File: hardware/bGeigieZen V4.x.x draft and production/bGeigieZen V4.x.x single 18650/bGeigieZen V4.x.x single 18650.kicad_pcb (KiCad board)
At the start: 2 copper layers, 129.4 x 64.6 mm, 13 parts, among them J1 M5 2x15 pin, J3 GPS, J4 Geiger Safepulse, J5 Extra support header, SW1 SW_SPDT

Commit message: Updated some more traces on the 4.x..x boards
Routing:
- net Net-(QIcharger1-Pin_1): track 31.7 -> 53.7 mm
- net Net-(BT1-+): track 67.9 -> 74.8 mm
- net Net-(BT1--): track 79.7 -> 78.9 mm
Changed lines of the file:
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@@
+	)
+	(segment
+		(start 199.356 84.642342)
+		(end 199.356 81.9844)
+		(width 0.5)
+		(layer "B.Cu")
+		(net 31)
 	)
 	(segment
@@
 	)
 	(segment
+		(start 182.7785 120.528)
+		(end 194.3292 120.528)
+		(width 0.5)
+		(layer "B.Cu")
+		(net 31)
+	)
+	(segment
 		(start 197.112 75.9648)
 		(end 200.6952 79.548)
@@
 	)
 	(segment
+		(start 186.0804 97.917942)
+		(end 199.356 84.642342)
+		(width 0.5)
+		(layer "B.Cu")
+		(net 31)
+	)
+	(segment
 		(start 200.6952 81.6696)
 		(end 203.86 78.5048)
@@
 	)
 	(segment
-		(start 199.356 115.5012)
-		(end 199.356 81.9844)
-		(width 0.5)
-		(layer "B.Cu")
-		(net 31)
-	)
-	(segment
 		(start 199.356 81.9844)
 		(end 198.0516 81.9844)
@@
 	)
 	(segment
-		(start 182.7785 120.528)
-		(end 194.3292 120.528)
+		(start 186.0804 112.2792)
+		(end 186.0804 97.917942)
 		(width 0.5)
 		(layer "B.Cu")
@@
 	(segment
 		(start 194.3292 120.528)
-		(end 199.356 115.5012)
+		(end 186.0804 112.2792)
 		(width 0.5)
 		(layer "B.Cu")
@@
 	)
 	(segment
+		(start 159.512 90.4736)
+		(end 150.0632 81.0248)
+		(width 0.25)
+		(layer "B.Cu")
+		(net 32)
+	)
+	(segment
+		(start 143.648 78.4848)
+		(end 146.198 81.0348)
+		(width 0.5)
+		(layer "B.Cu")
+		(net 32)
+	)
+	(segment
 		(start 149.342 75.9548)
 		(end 149.352 75.9448)
@@
 	)
 	(segment
-		(start 192.387642 102.474042)
-		(end 170.9384 81.0248)
+		(start 184.7596 110.102084)
+		(end 184.7596 93.4708)
 		(width 0.25)
 		(layer "B.Cu")
@@
 	)
 	(segment
+		(start 150.0632 81.0248)
+		(end 149.352 81.0248)
+		(width 0.25)
+		(layer "B.Cu")
+		(net 32)
+	)
+	(segment
+		(start 142.604 78.4848)
+		(end 143.648 78.4848)
+		(width 0.5)
+		(layer "B.Cu")
+		(net 32)
+	)
+	(segment
+		(start 181.7624 90.4736)
+		(end 159.512 90.4736)
+		(width 0.25)
+		(layer "B.Cu")
+		(net 32)
+	)
+	(segment
 		(start 182.707869 112.153815)
-		(end 192.387642 102.474042)
+		(end 184.7596 110.102084)
 		(width 0.25)
 		(layer "B.Cu")
@@
 	)
 	(segment
-		(start 170.9384 81.0248)
-		(end 149.352 81.0248)
+		(start 184.7596 93.4708)
+		(end 181.7624 90.4736)
 		(width 0.25)
 		(layer "B.Cu")
@@
 	)
 	(segment
+		(start 206.4397 123.5837)
+		(end 201.3089 123.5837)
+		(width 0.5)
+		(layer "B.Cu")
+		(net 33)
+	)
+	(segment
 		(start 205.181 95.9093)
 		(end 205.181 95.9092)
@@
 	)
 	(segment
+		(start 187.8076 110.0824)
+		(end 187.8076 99.7192)
+		(width 0.5)
+		(layer "B.Cu")
+		(net 33)
+	)
+	(segment
 		(start 205.181 95.9111)
 		(end 205.181 95.9101)
@@
 	)
 	(segment
-		(start 201.0156 100.259)
-		(end 205.181 96.0936)
-		(width 0.5)
-		(layer "B.Cu")
-		(net 33)
-	)
-	(segment
 		(start 205.181 95.9166)
 		(end 205.181 95.913)
@@
 	)
 	(segment
+		(start 187.8076 99.7192)
+		(end 189.9926 97.5342)
+		(width 0.5)
+		(layer "B.Cu")
+		(net 33)
+	)
+	(segment
 		(start 205.181 95.9101)
 		(end 205.181 95.9111)
@@
 	)
 	(segment
-		(start 205.181 96.0936)
+		(start 201.3089 123.5837)
+		(end 187.8076 110.0824)
+		(width 0.5)
+		(layer "B.Cu")
+		(net 33)
+	)
+	(segment
+		(start 205.181 96.093588)
 		(end 205.181 95.9166)
+		(width 0.5)
+		(layer "B.Cu")
+		(net 33)
+	)
+	(segment
+		(start 203.740388 97.5342)
+		(end 205.181 96.093588)
 		(width 0.5)
 		(layer "B.Cu")
@@
 	)
 	(segment
-		(start 201.0156 118.1596)
-		(end 201.0156 100.259)
-		(width 0.5)
-		(layer "B.Cu")
-		(net 33)
-	)
-	(segment
-		(start 206.4397 123.5837)
-		(end 201.0156 118.1596)
-		(width 0.5)
-		(layer "B.Cu")
+		(start 189.9926 97.5342)
+		(end 203.740388 97.5342)
+		(width 0.5)
+		(layer "B.Cu")

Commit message: Added Zen stickers and Safecast drive 0.5.0 app
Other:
- board text removed: "bGeigieZen V4.0.5 Draft"
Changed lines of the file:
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@@
 	(paper "A4")
 	(title_block
-		(title "bGeigieZen Draft V4.0.5")
-		(date "2024-06-07")
-		(rev "V4.0.5")
+		(title "bGeigieZen Draft V4.0.6")
+		(date "2024-06-29")
+		(rev "V4.0.6")
 	)
 	(layers
@@
 		)
 	)
-	(gr_text "bGeigieZen\nV4.0.5 Draft"
+	(gr_text "bGeigieZen\nV4.0.6 Draft"
 		(at 200.5584 112.724 90)
 		(layer "B.SilkS")

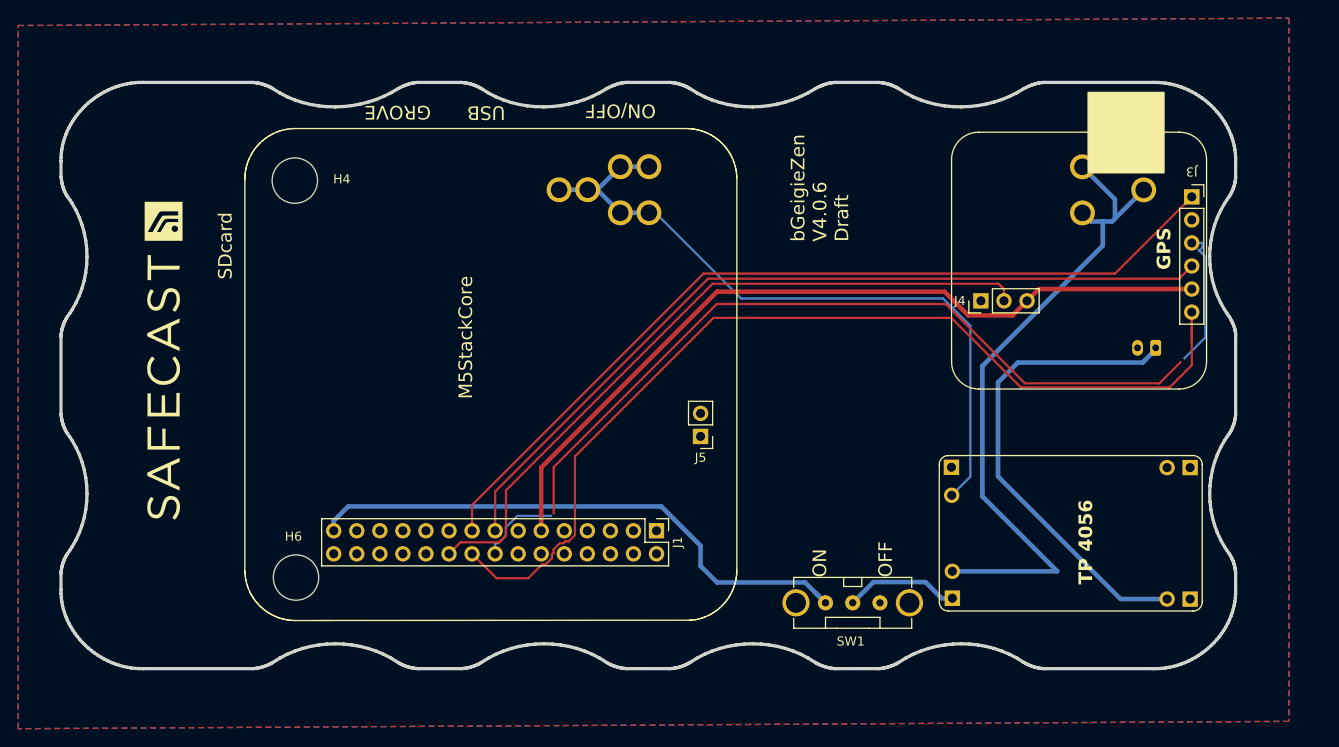
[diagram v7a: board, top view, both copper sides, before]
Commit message: Updated boards for Zen V4.0.7
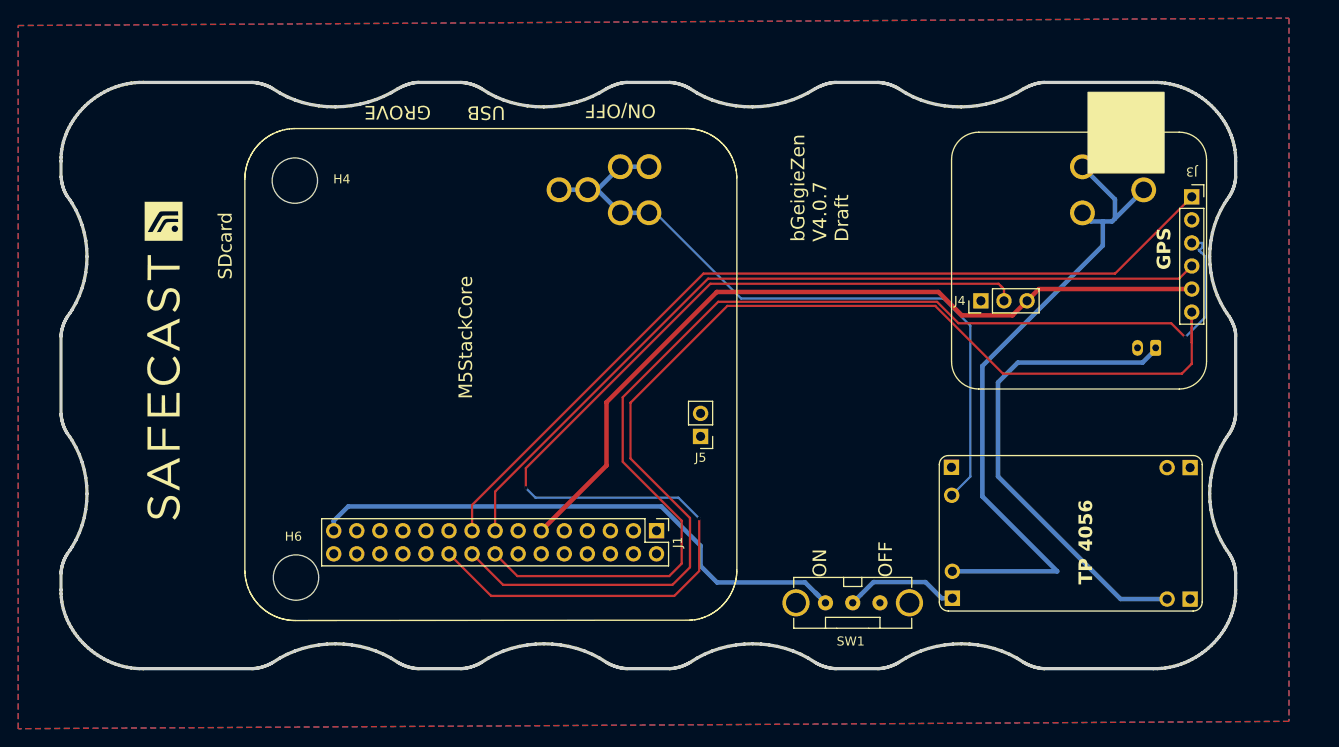
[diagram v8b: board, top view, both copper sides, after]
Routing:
- net /GIO2 on Core and GIO32 on Core-2: track 78.2 -> 121.7 mm, vias 0 -> 2
- net /SCL: track 110.0 -> 124.7 mm
- net /TX2: track 112.2 -> 124.5 mm, vias 2 -> 1
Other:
- board text added: "bGeigieZen V4.0.7 Draft"
- board text removed: "bGeigieZen V4.0.6 Draft"
